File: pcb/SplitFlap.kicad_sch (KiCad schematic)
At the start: 14 parts, among them U1 PCF8575DBR, U2 ULN2003

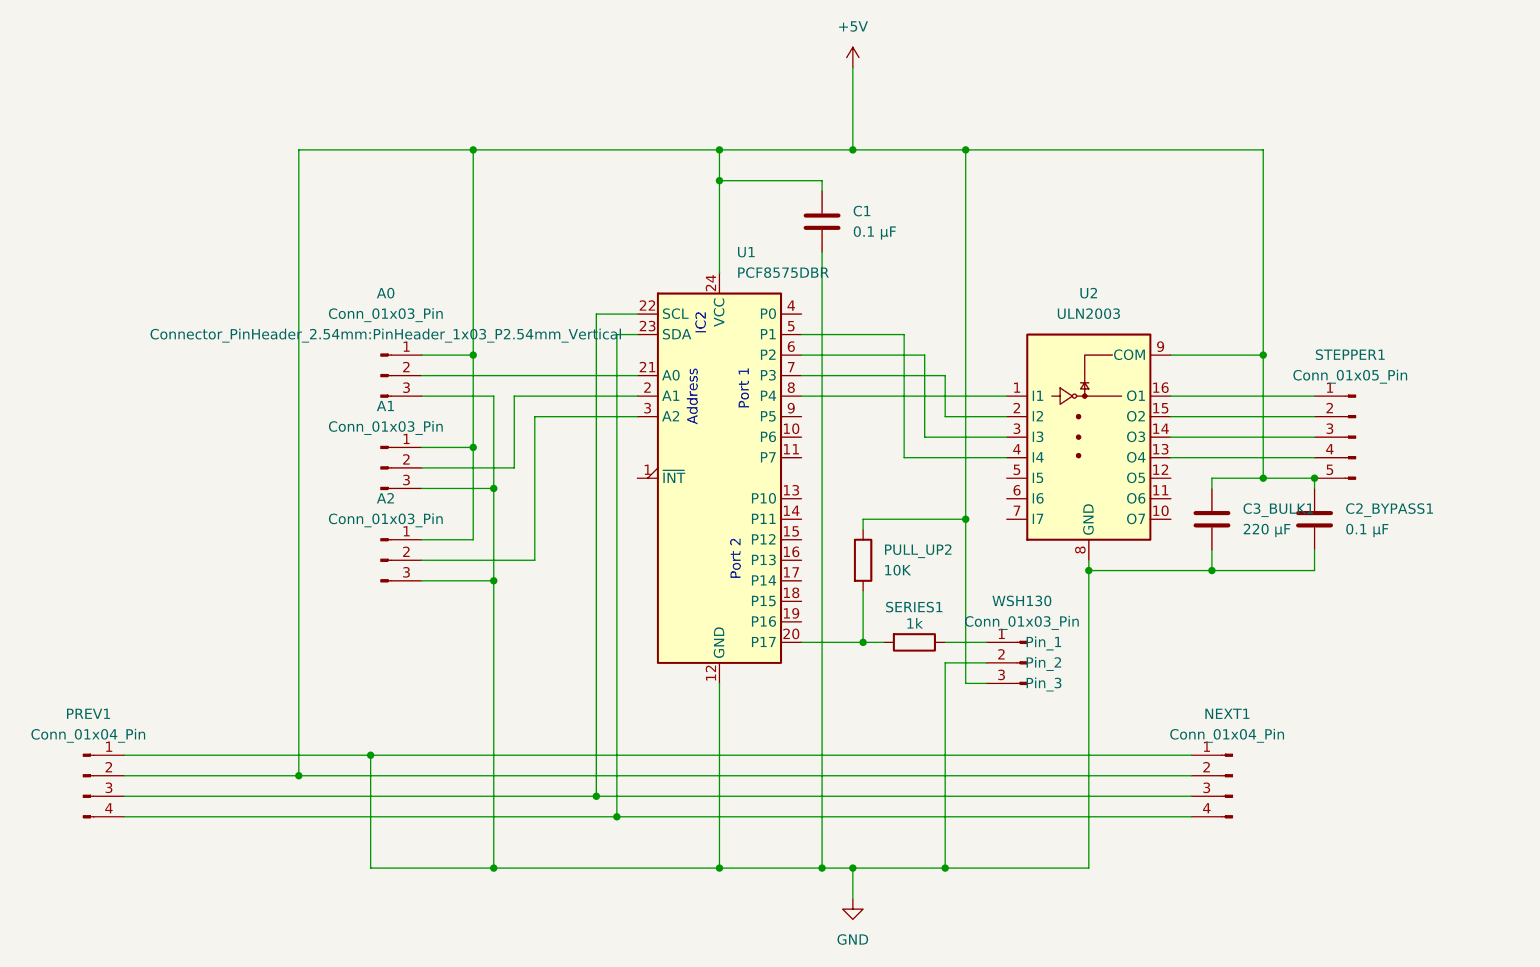
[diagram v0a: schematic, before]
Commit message: Add 3.3v line for PCF8575
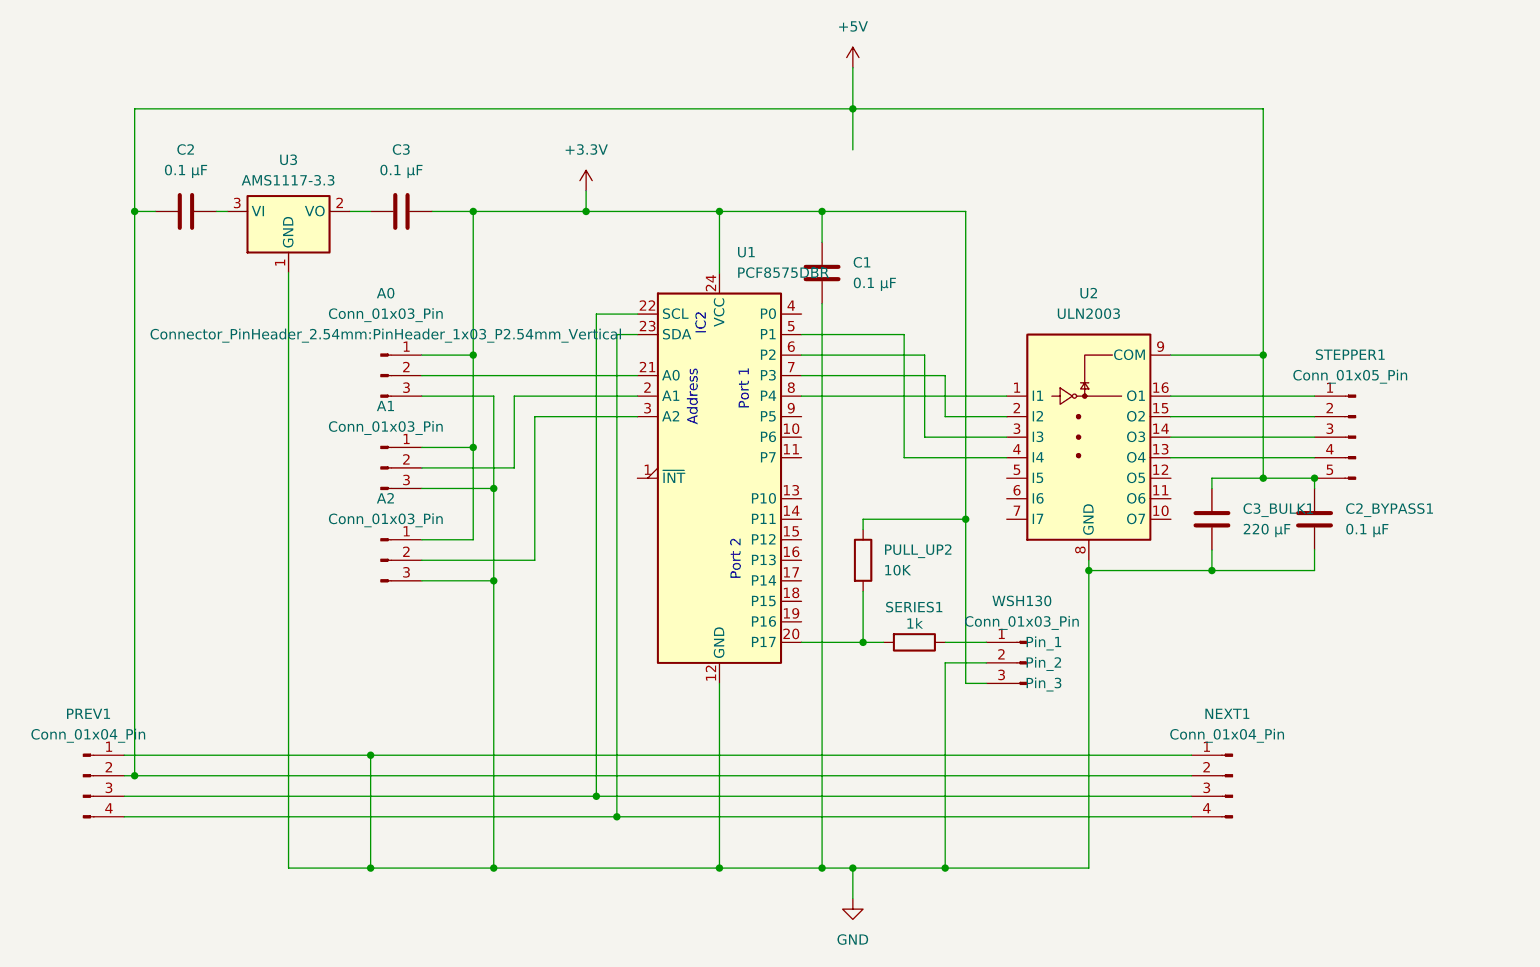
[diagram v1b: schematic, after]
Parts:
- added C2, C3: 0.1 µF, Capacitor_SMD:C_0402_1005Metric, symbol Device:C
- added U3: AMS1117-3.3, Package_TO_SOT_SMD:SOT-223-3_TabPin2, symbol Regulator_Linear:AMS1117-3.3
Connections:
- net +5V: now also C2.1; no longer A0.1 (Pin_1), A1.1 (Pin_1), A2.1 (Pin_1), C1.1, PULL_UP2.1, U1.24 (VCC), WSH130.3 (Pin_3)
- net GND: now also U3.1 (GND)
- new net: C3.1, U3.2 (VO)
- new net: C2.2, U3.3 (VI)
- new net +3.3V: A0.1 (Pin_1), A1.1 (Pin_1), A2.1 (Pin_1), C1.1, C3.2, PULL_UP2.1, U1.24 (VCC), WSH130.3 (Pin_3)
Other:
- moved on the sheet: C1

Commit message: Use two pin address connectors with pulldown resistor
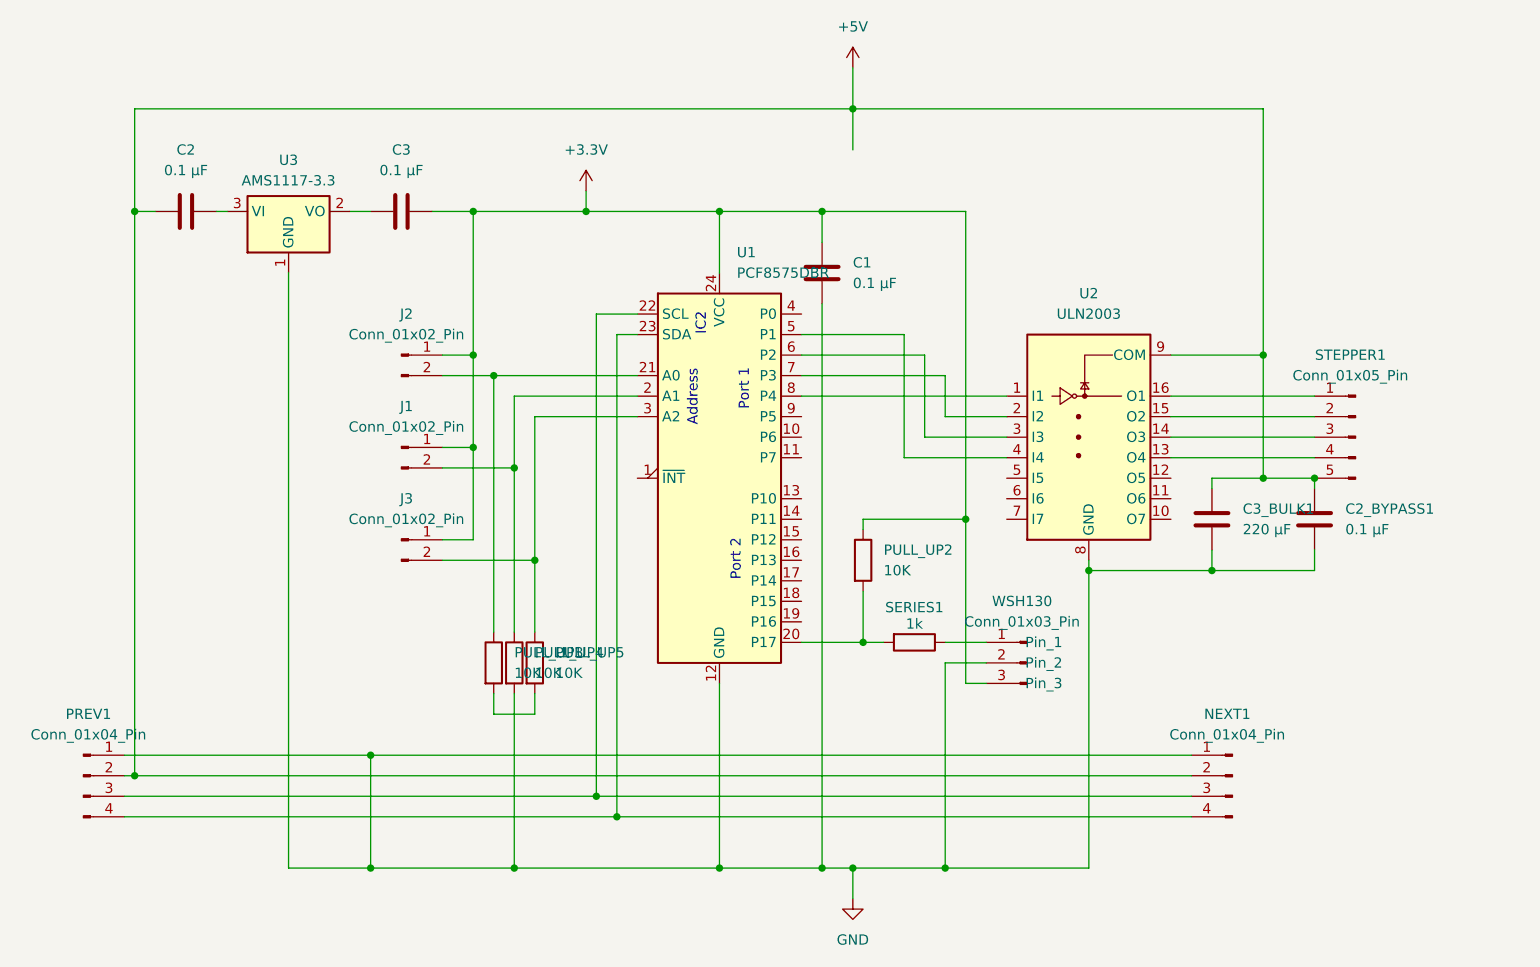
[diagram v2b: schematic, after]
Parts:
- removed A0, A1, A2: Conn_01x03_Pin, Connector_PinHeader_2.54mm:PinHeader_1x03_P2.54mm_Vertical, symbol Connector:Conn_01x03_Pin
- added J1, J2, J3: Conn_01x02_Pin, symbol Connector:Conn_01x02_Pin
- added PULL_UP3, PULL_UP4, PULL_UP5: 10K, Resistor_SMD:R_0603_1608Metric, symbol Device:R
- U3: MPN (none) -> C347222
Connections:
- net +3.3V: now also J1.1 (Pin_1), J2.1 (Pin_1), J3.1 (Pin_1)
- net GND: now also PULL_UP4.2
- net at U1.2 (A1): now also J1.2 (Pin_2), PULL_UP4.1
- net at U1.21 (A0): now also J2.2 (Pin_2), PULL_UP3.1
- net at U1.3 (A2): now also J3.2 (Pin_2), PULL_UP5.1
- new net: PULL_UP3.2, PULL_UP5.2

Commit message: Replace linear regulator with AP2112K
This regulator has a smaller footprint and seems to be better
optimised for our use case (more efficient, lower idle power draw,
less heat).
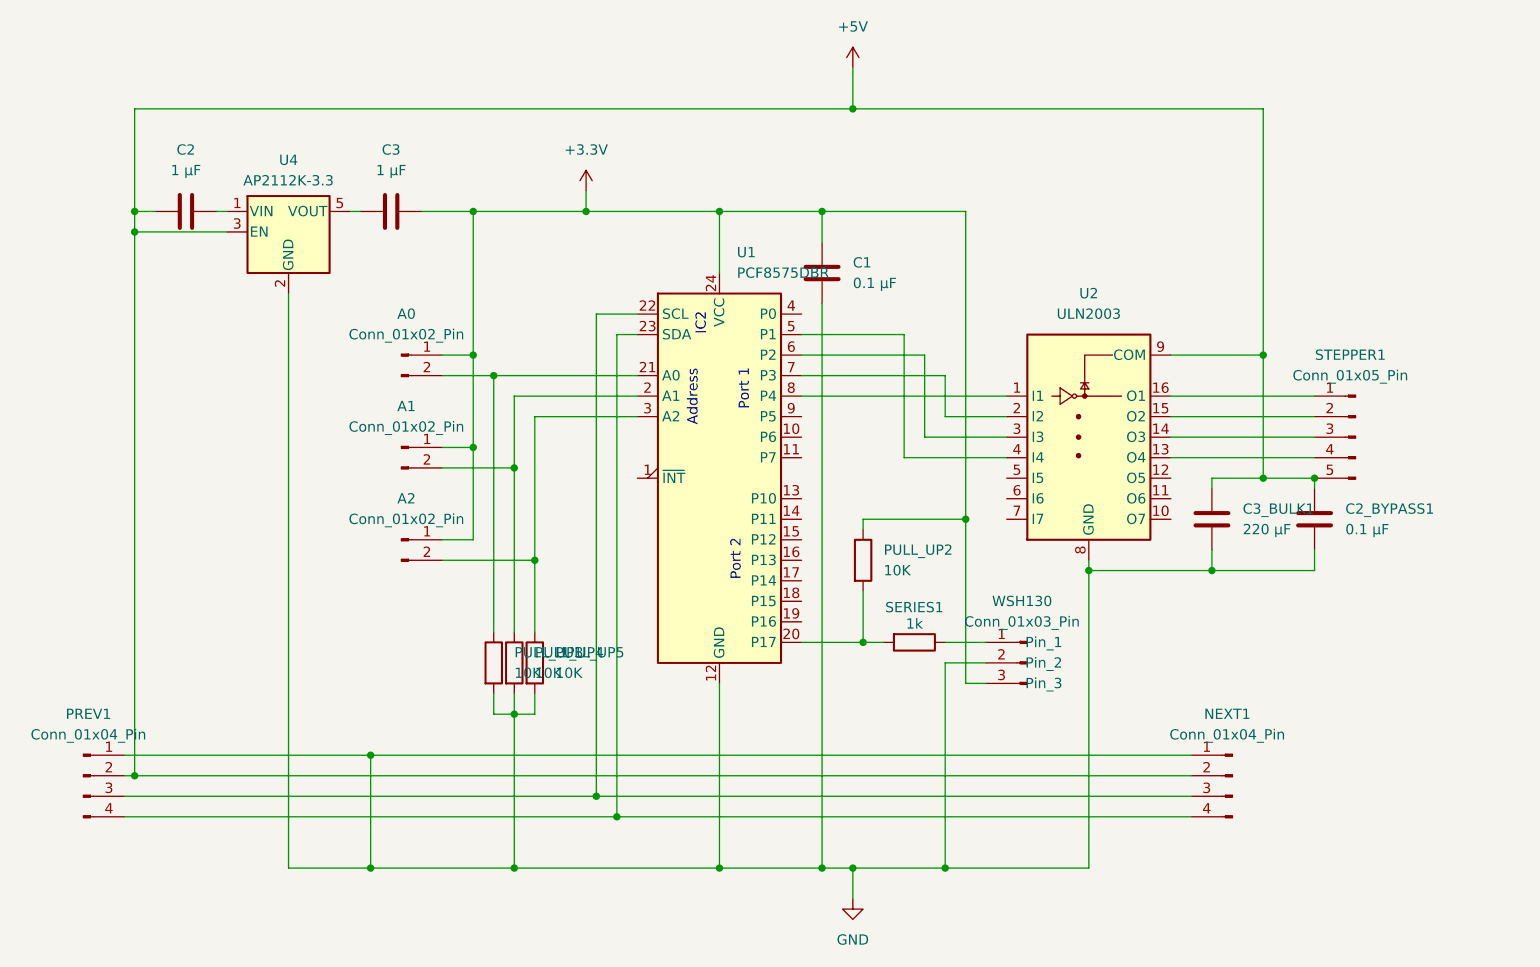
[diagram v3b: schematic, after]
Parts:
- removed U3: AMS1117-3.3, Package_TO_SOT_SMD:SOT-223-3_TabPin2, symbol Regulator_Linear:AMS1117-3.3
- added U4: AP2112K-3.3, Package_TO_SOT_SMD:SOT-23-5, symbol Regulator_Linear:AP2112K-3.3
- A0: renamed from J2; footprint (none) -> Connector_PinHeader_2.54mm:PinHeader_1x02_P2.54mm_Vertical
- A1: renamed from J1; footprint (none) -> Connector_PinHeader_2.54mm:PinHeader_1x02_P2.54mm_Vertical
- A2: renamed from J3; footprint (none) -> Connector_PinHeader_2.54mm:PinHeader_1x02_P2.54mm_Vertical
- C2, C3: value 0.1 µF -> 1 µF; footprint Capacitor_SMD:C_0402_1005Metric -> Capacitor_SMD:C_0603_1608Metric; MPN C6955083 -> C1592
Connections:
- net +5V: now also U4.3 (EN)
- net GND: now also PULL_UP3.2, PULL_UP5.2, U4.2 (GND)
- net at C3.1: now also U4.5 (VOUT)
- net at C2.2: now also U4.1 (VIN)
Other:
- moved on the sheet: C3

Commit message: Add missing part numbers
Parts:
- A0, A1, A2: MPN (none) -> C124375
- U4: MPN (none) -> C51118
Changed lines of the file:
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@@
+			)
+		)
+		(property "MPN" "C124375"
+			(at 86.36 101.6 0)
+			(effects
+				(font
+					(size 1.27 1.27)
+				)
+				(hide yes)
 			)
 		)
@@
 		)
 		(property "Description" "Generic connector, single row, 01x02, script generated"
+			(at 86.36 78.74 0)
+			(effects
+				(font
+					(size 1.27 1.27)
+				)
+				(hide yes)
+			)
+		)
+		(property "MPN" "C124375"
 			(at 86.36 78.74 0)
 			(effects
@@
 			)
 		)
+		(property "MPN" "C124375"
+			(at 86.36 90.17 0)
+			(effects
+				(font
+					(size 1.27 1.27)
+				)
+				(hide yes)
+			)
+		)
 		(pin "2"
 		)
@@
 			(at 72.39 63.5 0)
 			(effects
+				(font
+					(size 1.27 1.27)
+				)
+				(hide yes)
+			)
+		)
+		(property "MPN" "C51118"
+			(at 72.39 63.5 0)
+			(effects

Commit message: Add missing part number for address pins
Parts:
- A0, A1, A2: MPN C124375 -> C5383111
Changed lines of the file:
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@@
 			)
 		)
-		(property "MPN" "C124375"
+		(property "MPN" "C5383111"
 			(at 86.36 101.6 0)
 			(effects
@@
 			)
 		)
-		(property "MPN" "C124375"
+		(property "MPN" "C5383111"
 			(at 86.36 78.74 0)
 			(effects
@@
 			)
 		)
-		(property "MPN" "C124375"
+		(property "MPN" "C5383111"
 			(at 86.36 90.17 0)
 			(effects

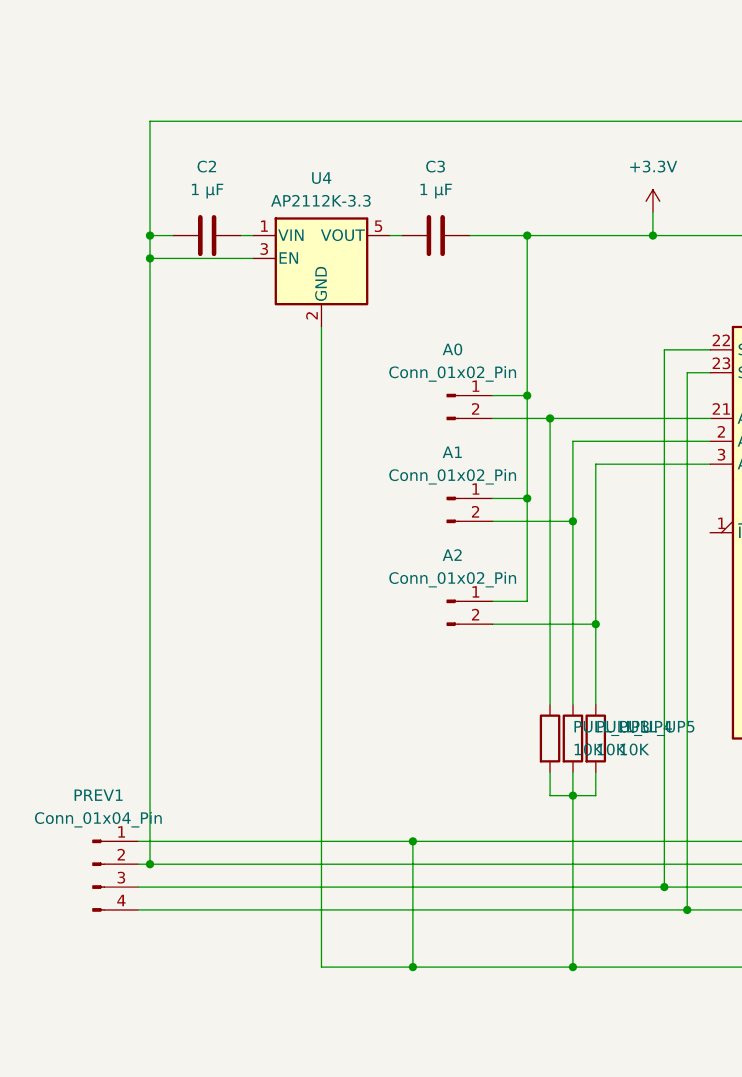
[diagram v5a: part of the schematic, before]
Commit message: Correct AP2112K capacitors
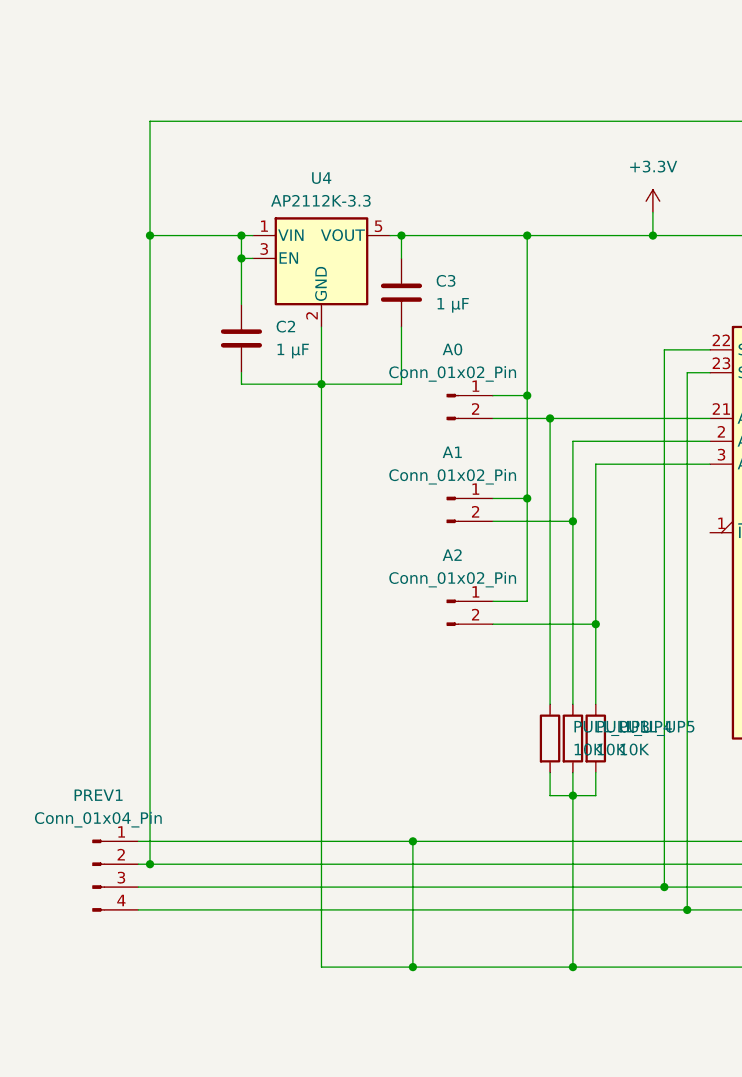
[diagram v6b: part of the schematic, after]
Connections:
- net +3.3V: now also U4.5 (VOUT)
- net +5V: now also C2.2, U4.1 (VIN); no longer C2.1
- net GND: now also C2.1, C3.1
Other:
- moved on the sheet: C2, C3
